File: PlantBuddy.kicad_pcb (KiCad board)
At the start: 4 copper layers, 31.6 x 36.1 mm, 42 parts, among them J1 USB_C_Receptacle_USB2.0, J2 C+, J3 C-, J4 External, Q1 DMG1012T, Q2 DMG1012T, SW1 SW_Push, U1 LTR-303ALS-01, U2 SHTC3, U3 ESP32-S3-WROOM-1-N8R8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

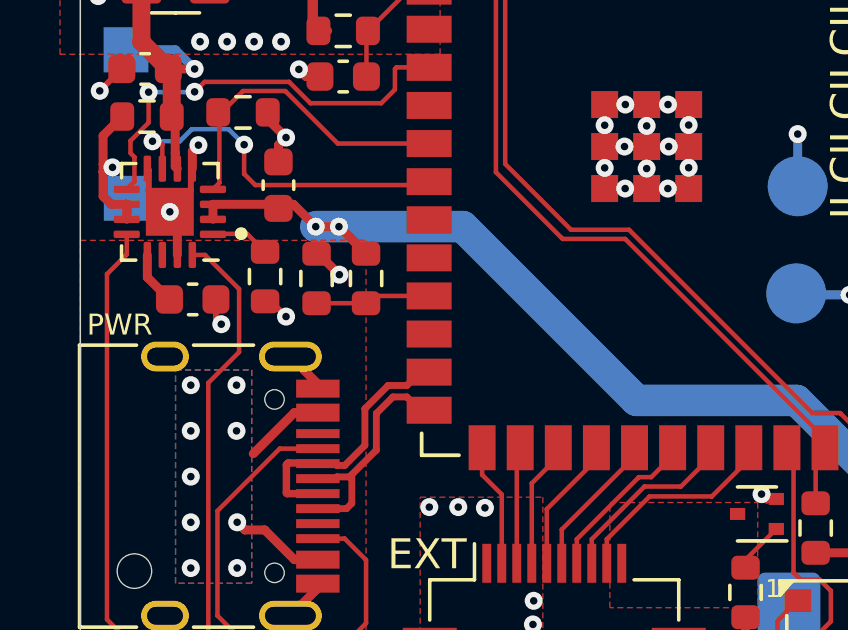
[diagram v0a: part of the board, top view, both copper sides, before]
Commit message: Moved temp mid to ADC1_CH8 & batsense to ADC1_CH7. To note: only ADC1 can be used if WiFi is enabled!
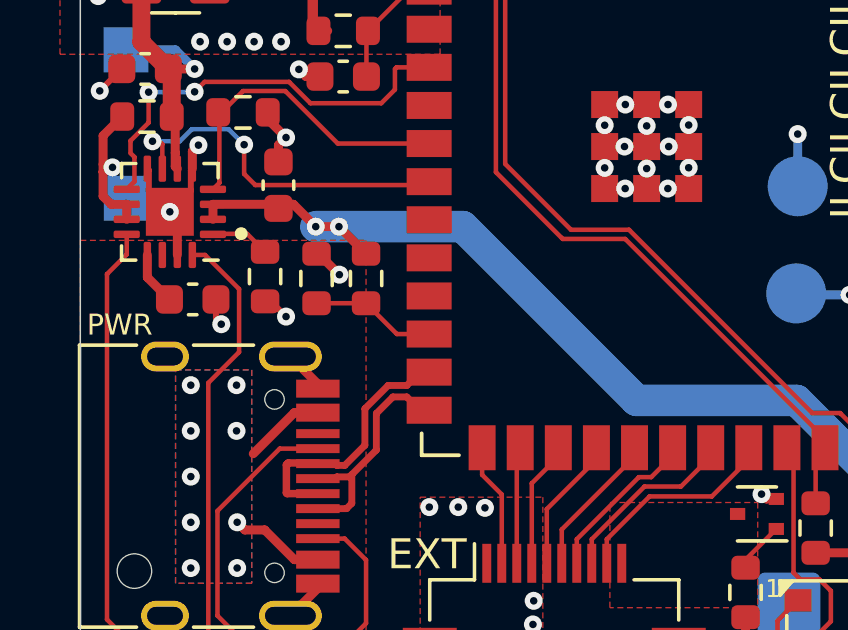
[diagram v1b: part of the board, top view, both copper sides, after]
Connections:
- U3 pad 11: /batsense -> unconnected-(U3-Pad11)
- U3 pad 12: unconnected-(U3-Pad12) -> /batsense
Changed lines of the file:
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@@
   (net 48 "unconnected-(U3-Pad9)")
   (net 49 "unconnected-(U3-Pad10)")
-  (net 50 "unconnected-(U3-Pad12)")
+  (net 50 "unconnected-(U3-Pad11)")
   (net 51 "/VGND")
   (net 52 "/EXT1")
@@
       (net 49 "unconnected-(U3-Pad10)") (pinfunction "IO17") (pintype "bidirectional"))
     (pad "11" smd rect locked (at -8.75 7.44) (size 1.5 0.9) (layers "F.Cu" "F.Paste" "F.Mask")
-      (net 22 "/batsense") (pinfunction "IO18") (pintype "bidirectional"))
+      (net 50 "unconnected-(U3-Pad11)") (pinfunction "IO18") (pintype "bidirectional"))
     (pad "12" smd rect locked (at -8.75 8.71) (size 1.5 0.9) (layers "F.Cu" "F.Paste" "F.Mask")
-      (net 50 "unconnected-(U3-Pad12)") (pinfunction "IO8") (pintype "bidirectional"))
+      (net 22 "/batsense") (pinfunction "IO8") (pintype "bidirectional"))
     (pad "13" smd rect locked (at -8.75 9.98) (size 1.5 0.9) (layers "F.Cu" "F.Paste" "F.Mask")
       (net 26 "/D-") (pinfunction "IO19") (pintype "bidirectional"))
@@
   (segment (start 128.55558 56.846671) (end 129.15558 57.446671) (width 0.1524) (layer "F.Cu") (net 21))
   (segment (start 130.87008 59.160171) (end 132.52108 59.160171) (width 0.1524) (layer "F.Cu") (net 22))
-  (segment (start 132.76408 58.917171) (end 132.52108 59.160171) (width 0.1524) (layer "F.Cu") (net 22))
-  (segment (start 134.62458 58.917171) (end 132.76408 58.917171) (width 0.1524) (layer "F.Cu") (net 22))
+  (segment (start 133.54808 60.187171) (end 134.62458 60.187171) (width 0.1524) (layer "F.Cu") (net 22))
+  (segment (start 132.52108 59.160171) (end 133.54808 60.187171) (width 0.1524) (layer "F.Cu") (net 22))
   (via (at 129.96908 40.941171) (size 0.6) (drill 0.25) (layers "F.Cu" "B.Cu") (net 24))
   (via (at 128.93908 40.931171) (size 0.6) (drill 0.25) (layers "F.Cu" "B.Cu") (net 24))

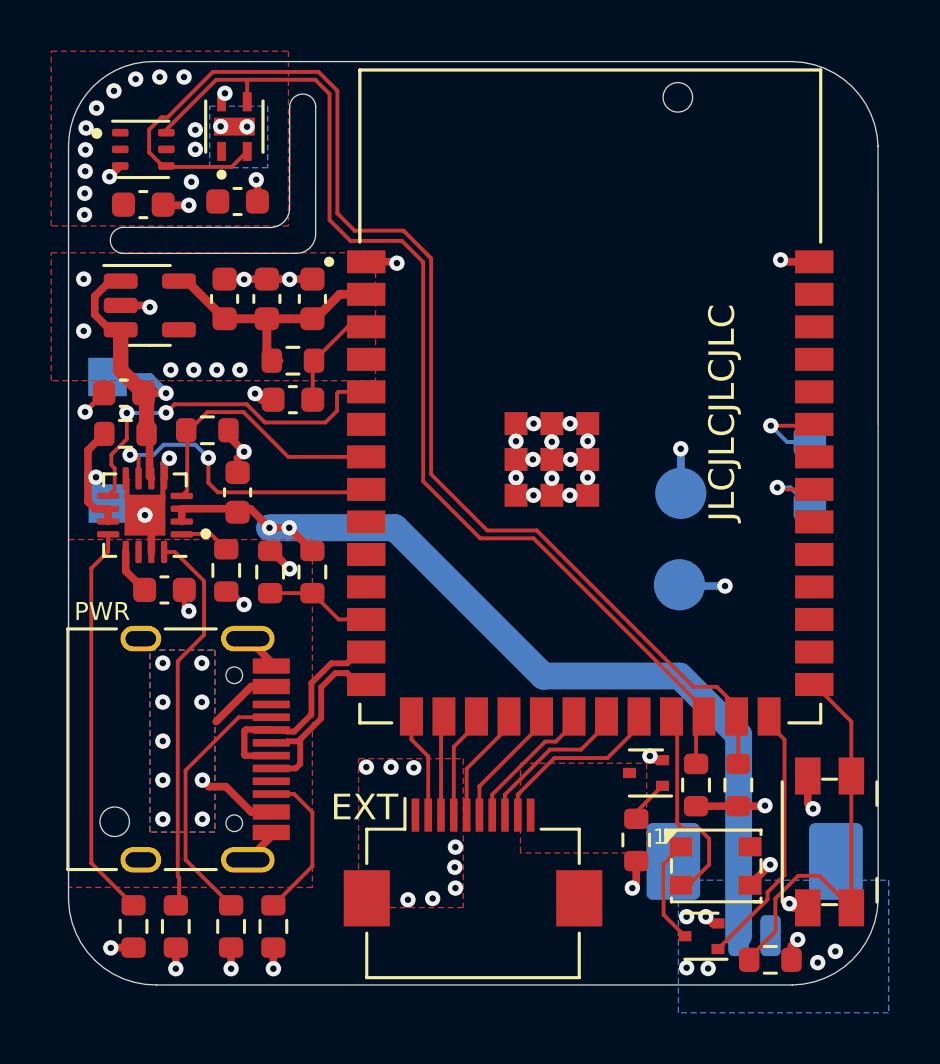
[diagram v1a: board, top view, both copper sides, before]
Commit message: Added power distribution switch for external connector
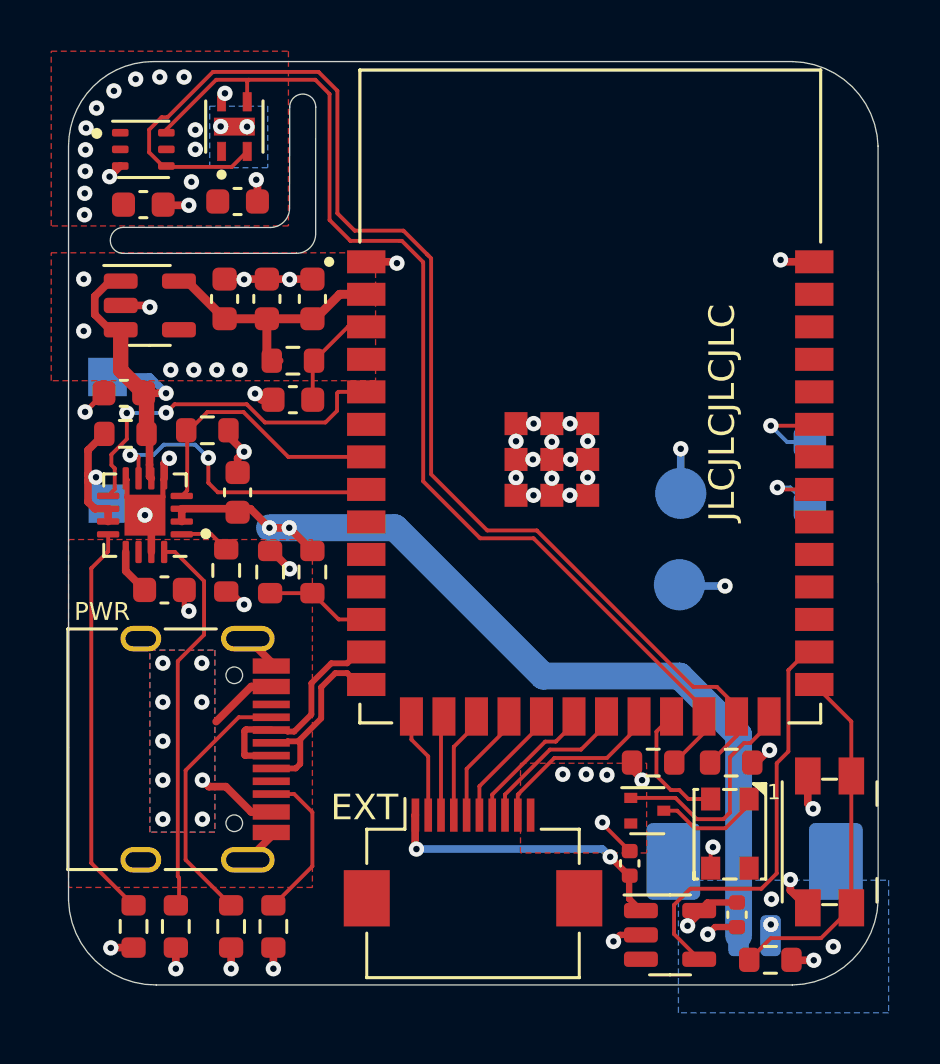
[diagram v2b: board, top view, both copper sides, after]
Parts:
- removed H1, H3: ToolingHole, Tooling:JLCPCB_Tooling_hole
- removed Q2: DMG1012T, Package_TO_SOT_SMD:SOT-523
- removed R12: 15k, Resistor_SMD:R_0603_1608Metric
- added C101: 100nF, Capacitor_SMD:C_0402_1005Metric, F.Cu at (149.1, 71.7)
- added C102: 100nF, Capacitor_SMD:C_0402_1005Metric, F.Cu at (144.9, 69.7)
- added U101: TPS2051B, Package_TO_SOT_SMD:SOT-23-5, F.Cu at (146.5, 72.5)
- moved Q1 5.34 mm to (145.6, 67.7), turned to 0 degrees
- moved R4 1.89 mm to (145.8, 65.8), turned to 180 degrees
- moved D1 1.36 mm to (148.9, 68.6), turned to 90 degrees
- moved R3 0.92 mm to (148.9, 65.8), turned to 0 degrees
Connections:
- J4 pad 1: +3V3 -> /EXT_VCC
- J4 pad 10: /VGND -> GND
- U3 pad 28: unconnected-(U3-Pad28) -> /EXT_EN
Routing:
- net /EXT_EN: track 1.72 -> 16.5 mm
- net /EXT_VCC: track 0.00 -> 11.7 mm, vias 0 -> 2
- net /status: track 8.19 -> 5.05 mm
- net GND: track 51.9 -> 54.2 mm, vias 44 -> 45
- net /btn: track 16.1 -> 14.2 mm
- net /EN_RGB: track 10.4 -> 8.85 mm
- net +3V3: track 16.9 -> 18.0 mm, vias 31 -> 25
- added copper zone on F.Cu, net GND
- removed copper zone on F.Cu, net /VGND

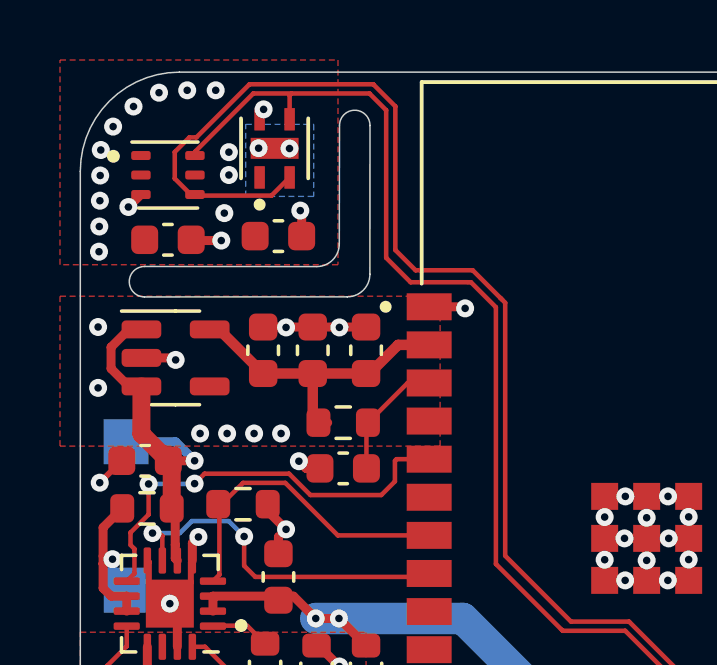
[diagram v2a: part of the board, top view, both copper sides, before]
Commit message: Changed 100nF capacitors to 0402
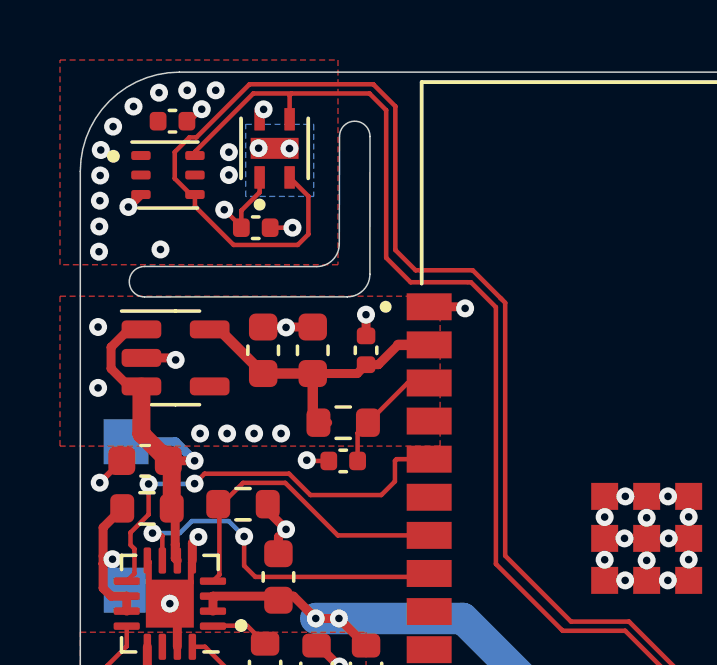
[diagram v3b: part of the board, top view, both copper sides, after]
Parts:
- C1, C2, C3, C8: footprint Capacitor_SMD:C_0603_1608Metric -> Capacitor_SMD:C_0402_1005Metric
- moved C2 3.96 mm to (126.1, 40.0)
- moved C1 0.81 mm to (128.8, 43.6)
- moved C3 0.25 mm to (131.8, 51.4)
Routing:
- net /SCL: track 49.8 -> 53.4 mm
- net +3V3: track 18.0 -> 20.8 mm, vias 25 -> 26
- net GND: track 54.2 -> 52.5 mm
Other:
- outline, holes or cut-outs redrawn

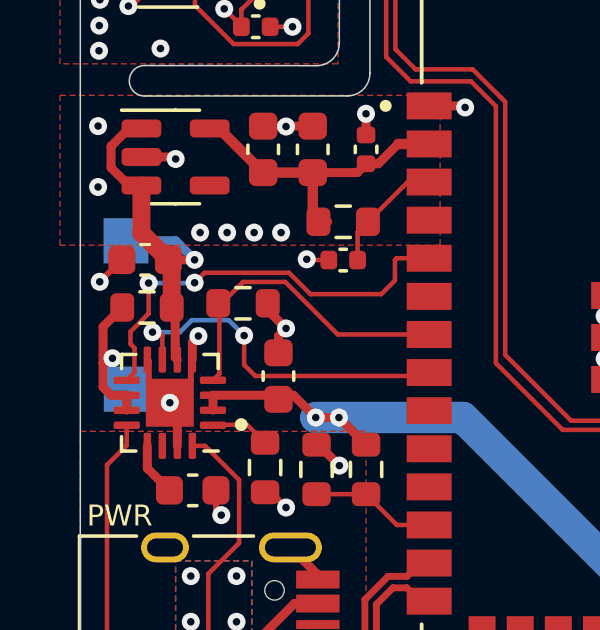
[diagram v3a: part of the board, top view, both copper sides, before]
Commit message: Removed current shunt & generated build files.
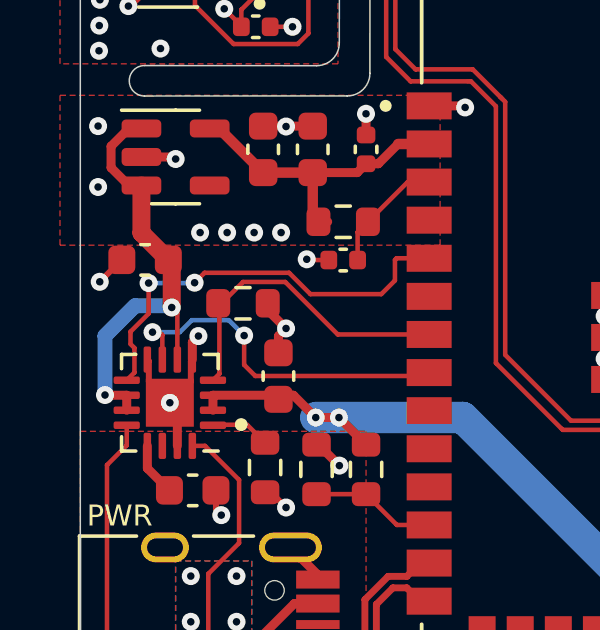
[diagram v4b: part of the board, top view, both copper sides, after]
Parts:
- removed J2: C+, TestPoint:TestPoint_Pad_1.5x1.5mm
- removed J3: C-, TestPoint:TestPoint_Pad_1.5x1.5mm
- removed R11: 100m, Resistor_SMD:R_0603_1608Metric
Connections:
- U4 pad 10: Net-(J2-Pad1) -> VCC
- U4 pad 11: Net-(J2-Pad1) -> VCC
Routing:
- net Net-(J2-Pad1): track 5.87 -> 0.00 mm, vias 1 -> 0
- net VCC: track 13.0 -> 15.4 mm, vias 1 -> 2
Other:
- board text removed: "Shunt - +"
- board text removed: "VCC"

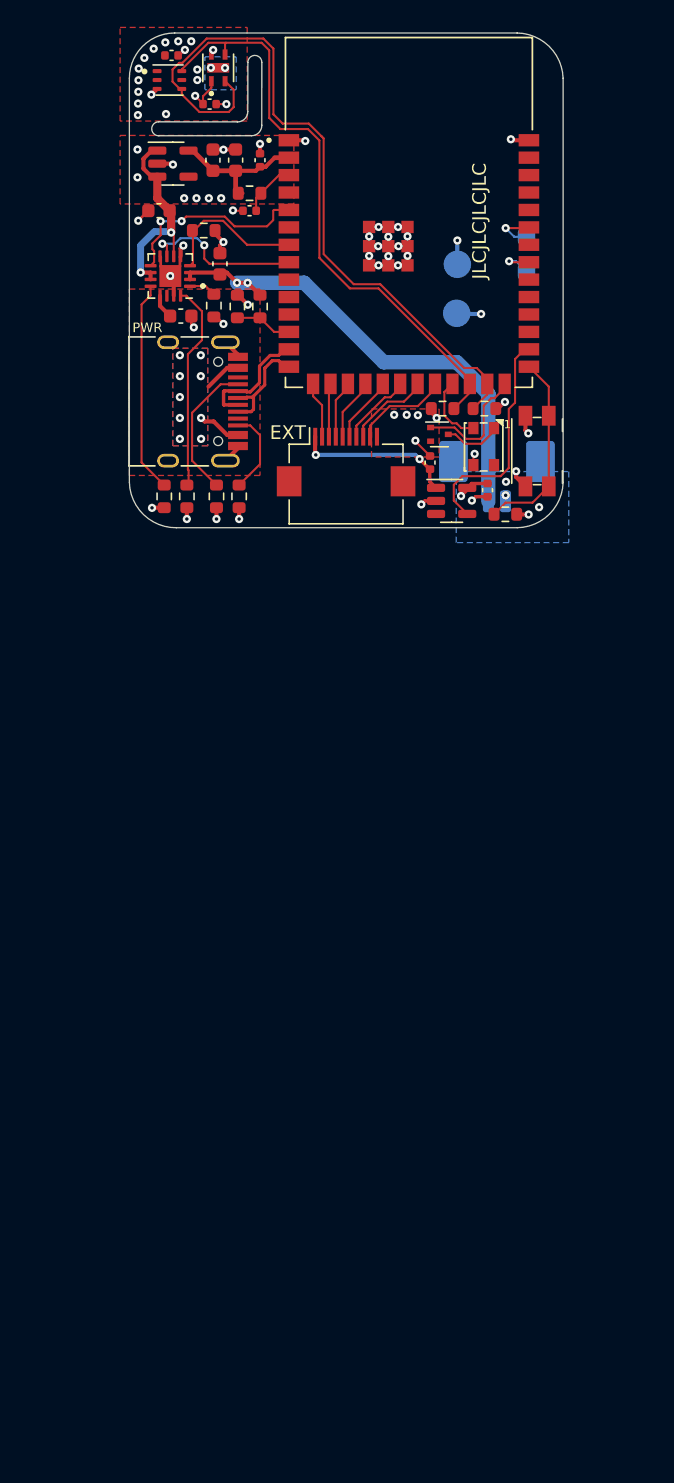
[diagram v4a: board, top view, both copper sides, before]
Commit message: Switched to ESP32-S3-Mini and changed PCB shape
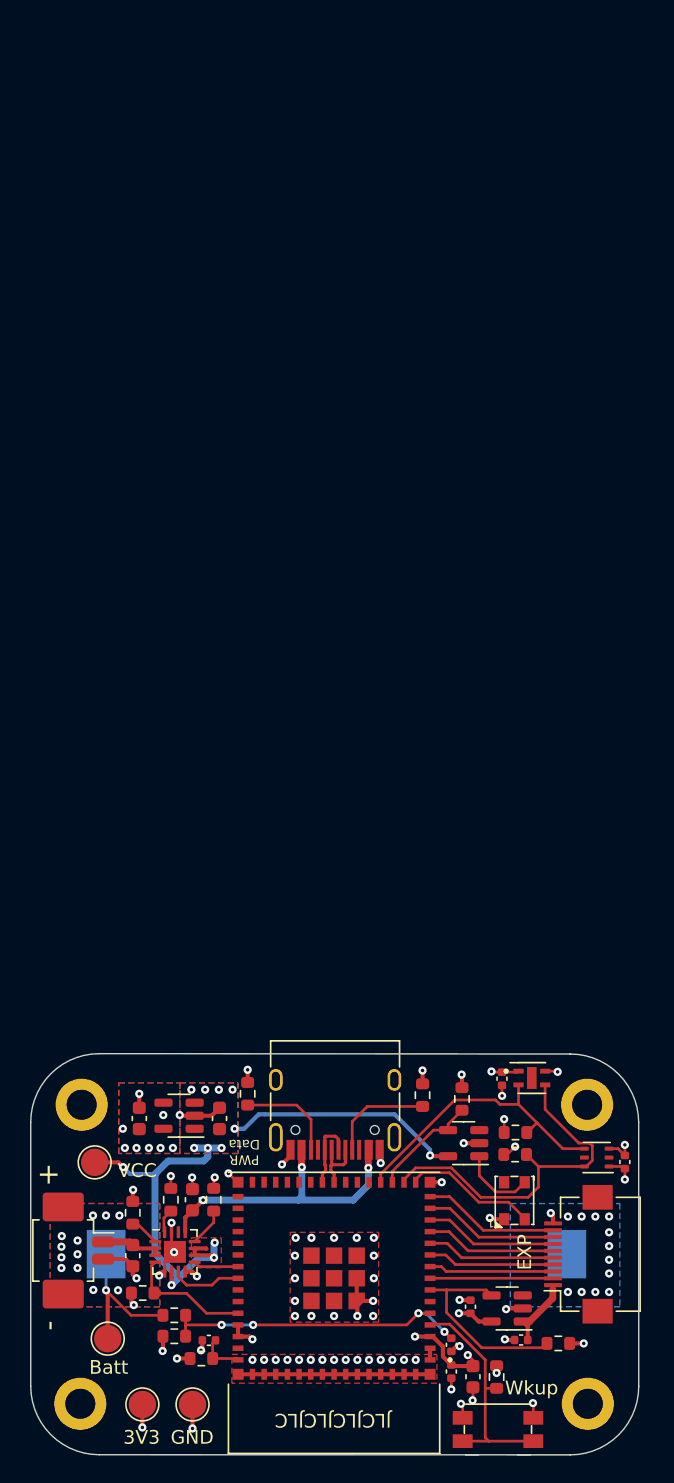
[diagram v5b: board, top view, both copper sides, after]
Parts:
- removed LS1: Speaker_Crystal, Piezo:Piezo
- removed Q1: DMG1012T, Package_TO_SOT_SMD:SOT-523
- removed U3: ESP32-S3-WROOM-1-N8R8, ESP32-S3:XCVR_ESP32S3WROOM1N8R8
- added C103: 100nF, Capacitor_SMD:C_0402_1005Metric, F.Cu at (146.5, 134.0)
- added H101: MountingHole, MountingHole:MountingHole_2.2mm_M2_DIN965_Pad, F.Cu at (119.4, 138.3)
- added H102: MountingHole, MountingHole:MountingHole_2.2mm_M2_DIN965_Pad, F.Cu at (119.5, 116.5)
- added H103: MountingHole, MountingHole:MountingHole_2.2mm_M2_DIN965_Pad, F.Cu at (156.4, 138.3)
- added H104: MountingHole, MountingHole:MountingHole_2.2mm_M2_DIN965_Pad, F.Cu at (156.4, 116.5)
- added J101: JST, Connector_Molex:Molex_PicoBlade_53261-0271_1x02-1MP_P1.25mm_Horizontal, F.Cu at (118.7, 127.2)
- added R101: 10k, Resistor_SMD:R_0603_1608Metric, F.Cu at (154.3, 133.9)
- added R102: 10k, Resistor_SMD:R_0603_1608Metric, F.Cu at (147.2, 116.1)
- added TP101: TestPoint, TestPoint:TestPoint_Pad_D2.0mm, F.Cu at (120.5, 120.7)
- added TP102: TestPoint, TestPoint:TestPoint_Pad_D2.0mm, F.Cu at (121.4, 133.6)
- added U102: ESP32-S3-MINI-1-N8, ESP32-S3-mini:XCVR_ESP32-S3-MINI-1-N8, F.Cu at (137.9, 129.2)
- added U103: TPS2051B, Package_TO_SOT_SMD:SOT-23-5, F.Cu at (147.4, 119.3)
- BT1: footprint Connector_Molex:Molex_PicoBlade_53261-0271_1x02-1MP_P1.25mm_Horizontal -> Keystone-2450:KEYSTONE_1052TR
- R10: value 5k1 -> 10k
- TP1, TP2: moved to F.Cu
- moved C9 90.4 mm to (148.0, 136.4), turned to -90 degrees
- moved C8 89.4 mm to (146.5, 136.0), turned to -90 degrees
- moved TP2 85.3 mm to (127.6, 138.4), turned to 0 degrees
- moved R8 85.0 mm to (128.2, 135.0)
- moved U1 84.5 mm to (157.1, 120.4), turned to 180 degrees
- moved C1 82.9 mm to (159.1, 120.7), turned to 90 degrees
- moved TP1 82.8 mm to (123.9, 138.4), turned to 0 degrees
- moved C3 82.4 mm to (128.8, 133.7)
- moved C2 78.4 mm to (150.2, 114.6), turned to -90 degrees
- moved R9 77.6 mm to (124.0, 130.3), turned to 0 degrees
- moved U2 77.1 mm to (152.3, 114.6), turned to 0 degrees
- moved R14 75.2 mm to (126.3, 133.4), turned to 180 degrees
- moved R13 73.8 mm to (126.3, 131.9), turned to 180 degrees
- moved C6 72.6 mm to (123.2, 127.5), turned to 90 degrees
- moved SW1 71.4 mm to (149.9, 140.2), turned to 180 degrees
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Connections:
- D1 pad 1: Net-(D1-Pad1) -> GND
- D1 pad 3: +3V3 -> Net-(D1-Pad3)
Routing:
- net /SCL: track 53.4 -> 21.6 mm
- net VCC: track 15.4 -> 46.4 mm, vias 2 -> 13
- net +BATT: track 35.8 -> 15.6 mm, vias 2 -> 13
- net /batsense: track 4.18 -> 22.9 mm, vias 0 -> 4
- net /SDA: track 43.5 -> 25.8 mm
- net VBUS: track 7.75 -> 21.8 mm, vias 9 -> 3
- net Net-(R6-Pad2): track 15.2 -> 1.77 mm
- net Net-(R5-Pad2): track 15.4 -> 2.80 mm
- net /~CHG: track 14.3 -> 3.30 mm, vias 2 -> 0
- net GND: track 52.5 -> 62.3 mm, vias 45 -> 79
- net /~PGOOD: track 12.0 -> 5.19 mm, vias 2 -> 0
- net /EXT_VCC: track 11.7 -> 5.35 mm, vias 2 -> 0
- net Net-(D1-Pad3): track 0.00 -> 5.51 mm
- net /EXT2: track 3.90 -> 9.11 mm
- net /EXT3: track 4.22 -> 9.25 mm
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- added copper zone on B.Cu, net +3V3
- added copper zone on B.Cu, net +BATT
- added copper zone on F.Cu, net +BATT
- added copper zone on B.Cu, net VCC
- added copper zone on F.Cu, net VCC
- removed copper zone on B.Cu, net VBUS
- removed copper zone on F.Cu, net VBUS
- removed copper zone on B.Cu, net unconnected-(U2-Pad5)
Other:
- board size 31.6 x 36.1 mm -> 44.3 x 29.2 mm
- board text added: "+"
- board text added: "-"
- board text added: "Batt"
- board text added: "EXP"
- board text added: "PWR Data"
- board text added: "VCC"
- board text added: "Wkup"
- board text removed: "+-"
- board text removed: "4-layer"
- board text removed: "Author:"
- board text removed: "Bat"
- board text removed: "Contact:"
- board text removed: "Călin-Petru Ardelean"
- board text removed: "EXT"
- board text removed: "PWR"
- board text removed: "ardelean.calin@proton.me"
